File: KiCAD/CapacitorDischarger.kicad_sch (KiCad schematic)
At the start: 44 parts, among them J1 SLB4-G-21, J2 SLB4-G-22, J3 MKDS5/2-9.5, J4 MKDS5/2-9.5, J5 DVM_Connector, Q1 MPSA42, Q2 STP10NK80Z 800V 9A

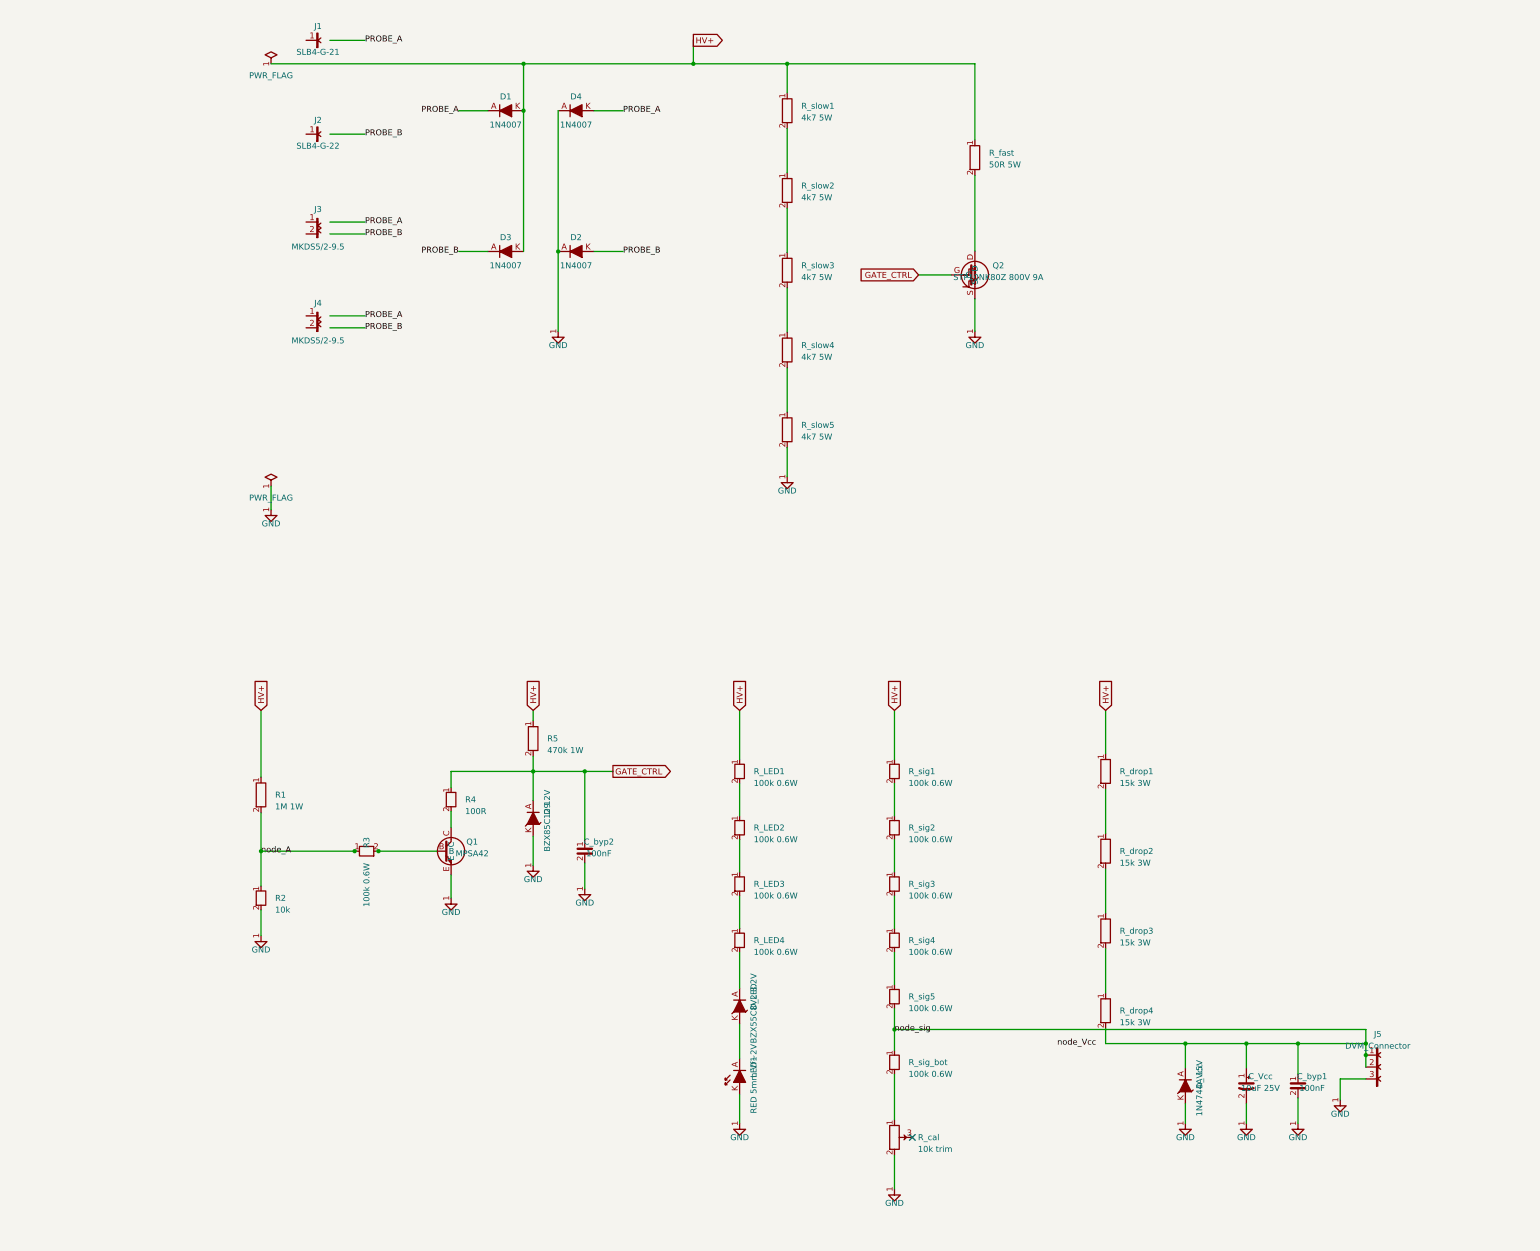
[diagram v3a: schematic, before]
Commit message: Fix symbol lib_ids and inner sub-symbol names for KiCad 10 compatibility
Schematic was generated with lib_ids that don't exist in KiCad 10,
causing 'symbol not found' on Update from Library and 'invalid symbol'
errors on sub-symbol name mismatches.

lib_id renames (pin numbers were already correct):
  Device:R_Large    → Device:R
  Device:R_POT      → Device:R_Potentiometer_Trim
  Device:CP         → Device:C_Polarized
  Device:Q_NPN_BCE  → Transistor_BJT:MPSA42  (E=1, B=2, C=3)
  Device:Q_NMOS_GDS → Transistor_FET:Q_NMOS_GDS  (G=1, D=2, S=3)

Inner sub-symbol names updated to match new lib_ids:
  CP_0/1_1 → C_Polarized_0/1_1
  R_POT_0/1_1 → R_Potentiometer_Trim_0/1_1
  Q_NPN_BCE_0/1_1 → MPSA42_0/1_1
  R_Large_0/1_1 → R_0/1_1 (duplicate Device:R entry removed)

Applied to all three schematic files.

Co-Authored-By: Claude Sonnet 4.6 <noreply@anthropic.com>
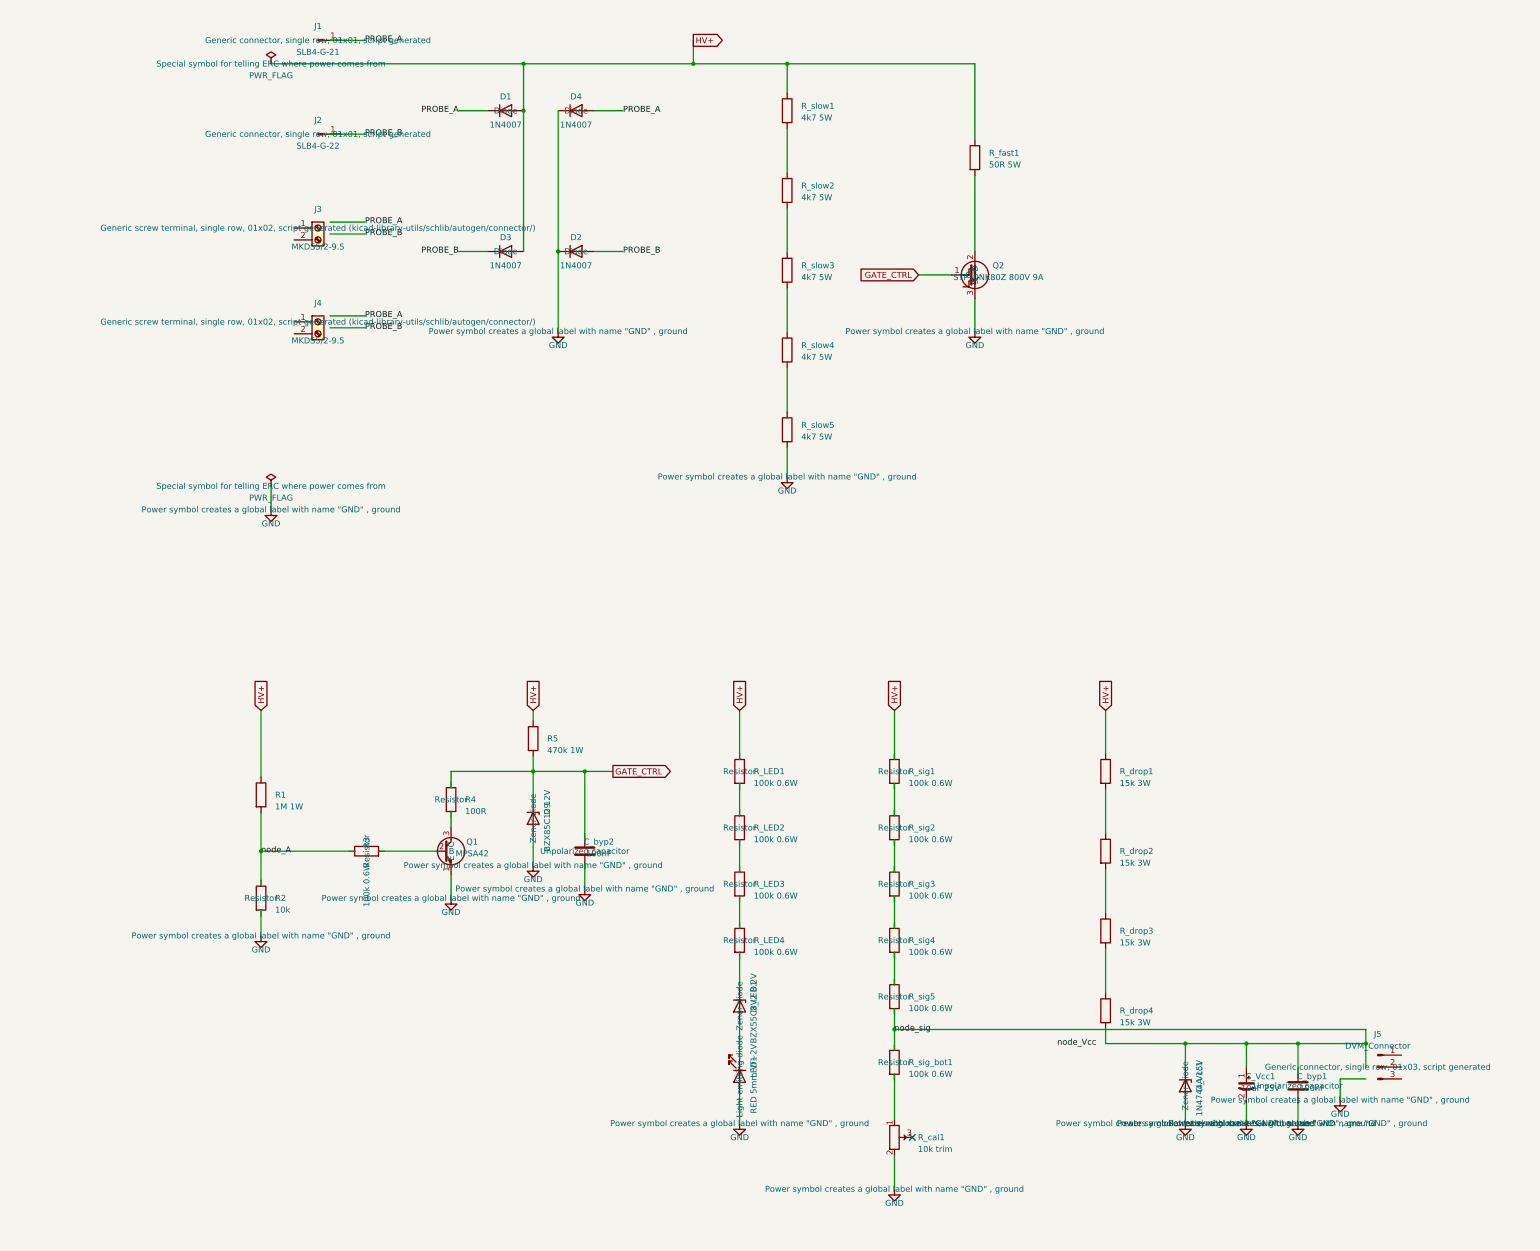
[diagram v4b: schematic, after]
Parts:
- C_Vcc1: renamed from C_Vcc; symbol Device:CP -> Device:C_Polarized
- Q1: symbol Device:Q_NPN_BCE -> Transistor_BJT:MPSA42
- Q2: symbol Device:Q_NMOS_GDS -> Transistor_FET:Q_NMOS_GDS
- R1, R5, R_drop1, R_drop2, R_drop3, R_drop4, R_slow1, R_slow2, R_slow3, R_slow4, R_slow5: symbol Device:R_Large -> Device:R
- R_cal1: renamed from R_cal; symbol Device:R_POT -> Device:R_Potentiometer_Trim
- R_fast1: renamed from R_fast; symbol Device:R_Large -> Device:R
- renumbered D_LED to D_LED1, D_Vcc to D_Vcc1, R_sig_bot to R_sig_bot1
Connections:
- net GATE_CTRL: now also D9.1 (K), Q2.1 (G); no longer C_byp2.1, D9.A, Q2.G, R4.1
- net GND: now also D2.1 (K), D4.1 (K), D9.2 (A), D_Vcc1.2 (A), LED1.2 (A), Q1.1 (E), Q2.3 (S); no longer C_byp1.2, C_byp2.2, D2.A, D4.A, D9.K, D_Vcc1.K, J5.3 (Pin_3), LED1.K, Q1.E, Q2.S, R2.2
- net HV+: now also D1.2 (A), D3.2 (A); no longer D1.K, D3.K, R_LED1.1, R_sig1.1
- net PROBE_A: now also D1.1 (K), D4.2 (A); no longer D1.A, D4.K
- net PROBE_B: now also D2.2 (A), D3.1 (K); no longer D2.K, D3.A
- net node_A: no longer R2.1, R3.1
- net node_sig: now also D_Vcc1.1 (K); no longer C_byp1.1, D_Vcc1.A, J5.1 (Pin_1), J5.2 (Pin_2), R_sig5.2, R_sig_bot1.1
- net at R_fast1.2: now also Q2.2 (D); no longer Q2.D
- net at R3.2: no longer Q1.B
- net at R4.2: no longer Q1.C
- net at R_LED1.2: no longer R_LED2.1
- net at R_LED2.2: no longer R_LED3.1
- net at R_LED3.2: no longer R_LED4.1
- net at R_LED4.2: no longer D_LED1.A
- net at R_sig1.2: no longer R_sig2.1
- net at R_sig2.2: no longer R_sig3.1
- net at R_sig3.2: no longer R_sig4.1
- net at R_sig4.2: no longer R_sig5.1
- net at R_sig_bot1.2: no longer R_cal1.1
- new net: D_LED1.2 (A), LED1.1 (K)
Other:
- moved on the sheet: J1, J2
